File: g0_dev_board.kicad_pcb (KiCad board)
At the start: 4 copper layers, 80 x 114 mm, 198 parts, among them J201 USB_B_Mini, J202 F103_SWD, J301 USB_B_Mini, J401 RJ45_Hanrun_HR911105A_Horizon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, J501 DM3AT-SF-PEJM5, J801 Uno_IOH, J802 Uno_IOL, J803 Uno_POWER, J804 Uno_ANALOG, J805 J_LA_L, J806 J_LA_R, Q201 MMBT3904, SW701 RESET, SW702 USER, U101 STM32G0B1CCT6, U201 USBLC6-2SC6, U202 AP7361C-33E, U203 STM32F103CBTx, U301 USBLC6-2SC6, U302 FT232RL, U401 W5500, U501 W25Q32JVSSIQ, U601 TMP100, U602 TMP100, Y101 32.768kHz CL7pF, Y201 8MHz, Y401 25MHz

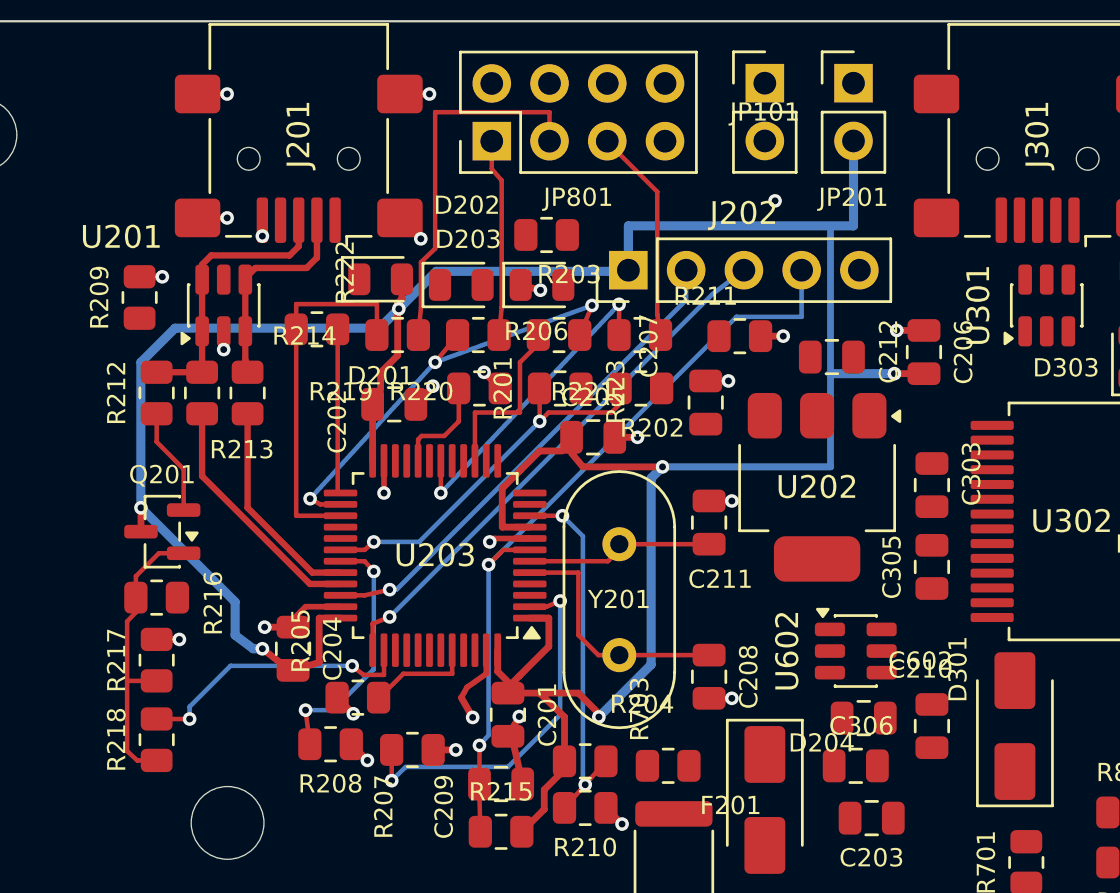
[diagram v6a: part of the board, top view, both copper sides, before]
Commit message: refactor(pcb): turn In2 into power plane with +3V3_STL island
По решению пользователя In2 стал слоем питания: +3.3V на всю плату и остров
+3V3_STL под ST-Link с выступом до JP201. In1 остаётся сплошной GND (опора
для F.Cu, дифпары не затронуты). Удалены 20 сегментов магистрали +3V3_STL на
B.Cu, которые замыкали область вокруг F103; питание выводов теперь через
переходные в остров. C206 возвращён к выводу 48. DRC: 0 нарушений.
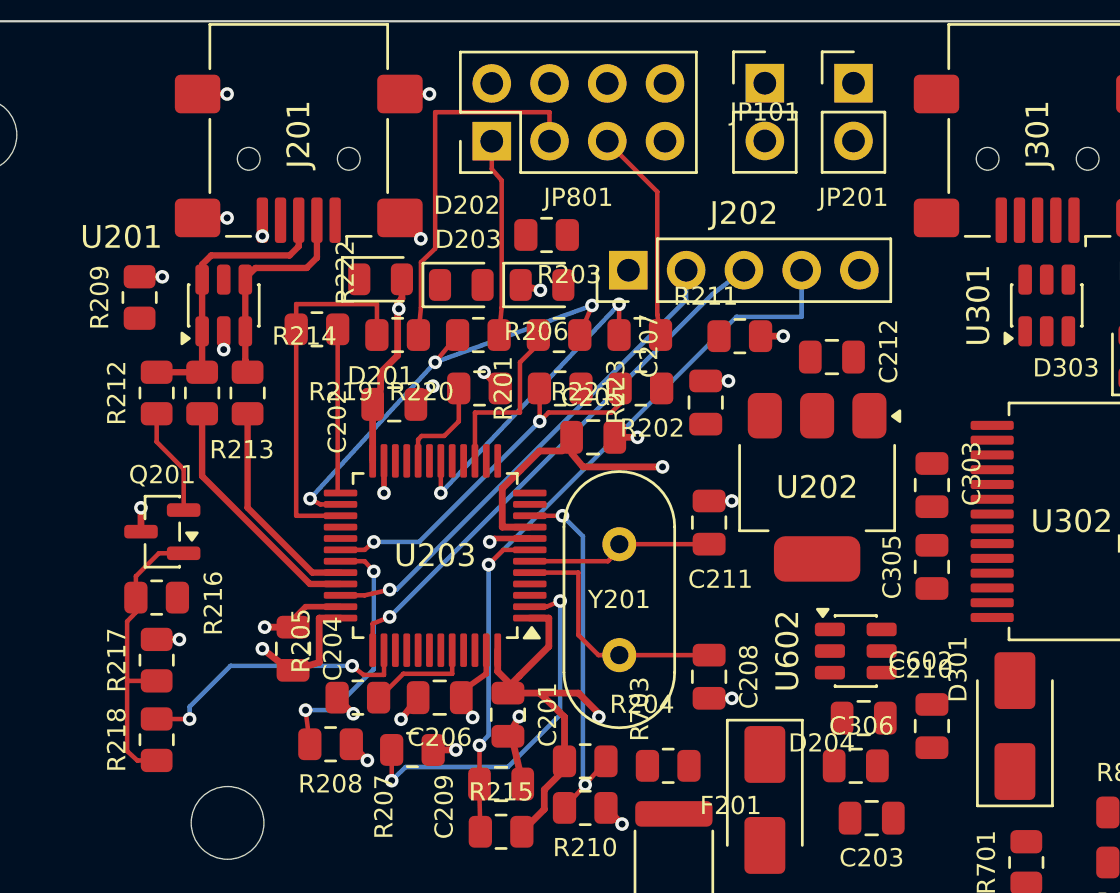
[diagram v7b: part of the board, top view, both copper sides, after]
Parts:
- moved C206 26.2 mm to (125.2, 65.8), turned to 0 degrees
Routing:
- net +3V3_STL: track 129.1 -> 42.2 mm
- net GND: track 35.6 -> 34.4 mm, vias 27 -> 25
- added copper zone on In2.Cu, net +3.3V
- added copper zone on In2.Cu, net +3V3_STL
- removed copper zone on In2.Cu, net GND
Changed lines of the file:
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@@
 	(footprint "Capacitor_SMD:C_0805_2012Metric"
 		(layer "F.Cu")
-		(at 146.5 50.55 90)
+		(at 125.2 65.75)
 		(descr "Capacitor SMD 0805 (2012 Metric), square (rectangular) end terminal, IPC-7351 nominal, (Body size source: IPC-SM-782 page 76, https://www.pcb-3d.com/wordpress/wp-content/uploads/ipc-sm-782a_amendment_1_and_2.pdf, https://docs.google.com/spreadsheets/d/1BsfQQcO9C6DZCsRaXUlFlo91Tg2WpOkGARC1WS5S8t0/edit?usp=sharing)")
 		(tags "capacitor")
 		(property "Reference" "C206"
-			(at 0 1.75 270)
+			(at 0 1.75 180)
 			(layer "F.SilkS")
 			(effects
@@
 		)
 		(property "Value" "4.7u"
-			(at 0 1.68 90)
+			(at 0 1.68 0)
 			(layer "F.Fab")
 			(effects
@@
 		)
 		(property "Datasheet" ""
-			(at 0 0 90)
+			(at 0 0 0)
 			(layer "F.Fab")
 			(hide yes)
@@
 		)
 		(property "Description" "Unpolarized capacitor"
-			(at 0 0 90)
+			(at 0 0 0)
 			(layer "F.Fab")
 			(hide yes)
@@
 		)
 		(property "KiLib_Generator" "SMD_2terminal_chip_molded"
-			(at 0 0 90)
+			(at 0 0 0)
 			(layer "F.SilkS")
 			(hide yes)
@@
 		)
 		(property "LCSC" "C1779"
-			(at 0 0 90)
+			(at 0 0 0)
 			(layer "F.SilkS")
 			(hide yes)
@@
 		)
 		(fp_text user "${REFERENCE}"
-			(at 0 0 90)
+			(at 0 0 0)
 			(layer "F.Fab")
 			(effects
@@
 		)
 		(pad "1" smd roundrect
-			(at -0.95 0 90)
+			(at -0.95 0)
 			(size 1 1.45)
 			(layers "F.Cu" "F.Mask" "F.Paste")
@@
 		)
 		(pad "2" smd roundrect
-			(at 0.95 0 90)
+			(at 0.95 0)
 			(size 1 1.45)
 			(layers "F.Cu" "F.Mask" "F.Paste")
@@
 	)
 	(segment
+		(start 124.25 65.75)
+		(end 123.5 66.7)
+		(width 0.3)
+		(layer "F.Cu")
+		(net "+3V3_STL")
+	)
+	(segment
 		(start 119.9 62.25)
 		(end 119.9 64.2)
@@
 	)
 	(segment
-		(start 146.5 51.5)
-		(end 145.2 51.5)
-		(width 0.3)
-		(layer "F.Cu")
-		(net "+3V3_STL")
-	)
-	(segment
 		(start 123.54 48.2)
 		(end 123.35 48.4)
@@
 	)
 	(via
-		(at 145.2 51.5)
-		(size 0.6)
-		(drill 0.3)
-		(layers "F.Cu" "B.Cu")
-		(net "+3V3_STL")
-	)
-	(via
 		(at 135 55.6)
 		(size 0.6)
@@
 		(net "+3V3_STL")
 	)
-	(segment
-		(start 145.2 51.5)
-		(end 142.39 51.5)
-		(width 0.4)
-		(layer "B.Cu")
-		(net "+3V3_STL")
-	)
-	(segment
-		(start 132.199999 66.599999)
-		(end 134.5 64.3)
-		(width 0.4)
-		(layer "B.Cu")
-		(net "+3V3_STL")
-	)
-	(segment
-		(start 112.06 51)
-		(end 113.56 49.5)
-		(width 0.4)
-		(layer "B.Cu")
-		(net "+3V3_STL")
-	)
-	(segment
-		(start 125.05 47)
-		(end 132.65 47)
-		(width 0.4)
-		(layer "B.Cu")
-		(net "+3V3_STL")
-	)
-	(segment
-		(start 116.2 63)
-		(end 117 63.6)
-		(width 0.4)
-		(layer "B.Cu")
-		(net "+3V3_STL")
-	)
-	(segment
-		(start 133.5 46.95)
-		(end 133.5 45)
-		(width 0.4)
-		(layer "B.Cu")
-		(net "+3V3_STL")
-	)
-	(segment
-		(start 142.39 55.6)
-		(end 142.39 45)
-		(width 0.3)
-		(layer "B.Cu")
-		(net "+3V3_STL")
-	)
-	(segment
-		(start 143.4 45)
-		(end 143.4 41.265)
-		(width 0.4)
-		(layer "B.Cu")
-		(net "+3V3_STL")
-	)
-	(segment
-		(start 117 63.6)
-		(end 117.4 63.6)
-		(width 0.4)
-		(layer "B.Cu")
-		(net "+3V3_STL")
-	)
-	(segment
-		(start 112.06 57.4)
-		(end 112.06 51)
-		(width 0.4)
-		(layer "B.Cu")
-		(net "+3V3_STL")
-	)
-	(segment
-		(start 133.5 45)
-		(end 143.4 45)
-		(width 0.4)
-		(layer "B.Cu")
-		(net "+3V3_STL")
-	)
-	(segment
-		(start 134.5 56.1)
-		(end 135 55.6)
-		(width 0.4)
-		(layer "B.Cu")
-		(net "+3V3_STL")
-	)
-	(segment
-		(start 113.56 49.5)
-		(end 122.55 49.5)
-		(width 0.4)
-		(layer "B.Cu")
-		(net "+3V3_STL")
-	)
-	(segment
-		(start 116.2 61.54)
-		(end 116.2 63)
-		(width 0.4)
-		(layer "B.Cu")
-		(net "+3V3_STL")
-	)
-	(segment
-		(start 123.4 48.65)
-		(end 125.05 47)
-		(width 0.4)
-		(layer "B.Cu")
-		(net "+3V3_STL")
-	)
-	(segment
-		(start 135 55.6)
-		(end 142.39 55.6)
-		(width 0.3)
-		(layer "B.Cu")
-		(net "+3V3_STL")
-	)
-	(segment
-		(start 112.06 57.4)
-		(end 116.2 61.54)
-		(width 0.4)
-		(layer "B.Cu")
-		(net "+3V3_STL")
-	)
-	(segment
-		(start 134.5 64.3)
-		(end 134.5 56.1)
-		(width 0.4)
-		(layer "B.Cu")
-		(net "+3V3_STL")
-	)
-	(segment
-		(start 132.65 47)
-		(end 133.5 46.95)
-		(width 0.4)
-		(layer "B.Cu")
-		(net "+3V3_STL")
-	)
-	(segment
-		(start 122.55 49.5)
-		(end 123.4 48.65)
-		(width 0.4)
-		(layer "B.Cu")
+	(via
+		(at 123.5 66.7)
+		(size 0.6)
+		(drill 0.3)
+		(layers "F.Cu" "B.Cu")
 		(net "+3V3_STL")
 	)
@@
 	)
 	(segment
-		(start 146.5 49.6)
-		(end 145.3 49.6)
-		(width 0.3)
-		(layer "F.Cu")
-		(net "GND")
-	)
-	(segment
 		(start 115.7 49.638)
 		(end 115.7 50.44)
@@
 	)
 	(via
-		(at 139.95 43.9)
-		(size 0.6)
-		(drill 0.3)
-		(layers "F.Cu" "B.Cu")
-		(net "GND")
-	)
-	(via
 		(at 138.05 57.1)
 		(size 0.6)
@@
 	)
 	(via
-		(at 145.3 49.6)
-		(size 0.6)
-		(drill 0.3)
-		(layers "F.Cu" "B.Cu")
-		(net "GND")
-	)
-	(via
 		(at 138.05 65.78)
 		(size 0.6)
@@
 	)
 	(zone
-		(net "GND")
+		(net "+3.3V")
 		(layer "In2.Cu")
 		(hatch edge 0.5)
@@
 		(polygon
 			(pts
-				(xy 100.3 36.3) (xy 179.7 36.3) (xy 179.7 149.7) (xy 100.3 149.7)
+				(xy 100.3 36.3) (xy 110 36.3) (xy 110 73.1) (xy 137 73.1) (xy 137 46.2) (xy 145.2 46.2) (xy 145.2 39.3)
+				(xy 141.4 39.3) (xy 141.4 42.4) (xy 137 42.4) (xy 137 36.3) (xy 179.7 36.3) (xy 179.7 149.7) (xy 100.3 149.7)
+			)
+		)
+	)
+	(zone
+		(net "+3V3_STL")
+		(layer "In2.Cu")
+		(hatch edge 0.5)
+		(connect_pads
+			(clearance 0.25)
+		)
+		(min_thickness 0.2)
+		(fill
+			(thermal_gap 0.5)
+			(thermal_bridge_width 0.5)
+			(island_removal_mode 0)
+		)
+		(polygon
+			(pts
+				(xy 110.6 36.3) (xy 136.4 36.3) (xy 136.4 43) (xy 142 43) (xy 142 39.9) (xy 144.6 39.9) (xy 144.6 45.6)
+				(xy 136.4 45.6) (xy 136.4 72.5) (xy 110.6 72.5)
 			)
 		)

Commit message: feat(pcb): rework ST-Link LED cluster and JP801 SWD lines
R201/R202/R211 перенесены к светодиодам у верхнего края (R201/R202
вертикально), D201/D202 сдвинуты; D203/R203 (индикатор основной +3.3V)
перенесены к LDO, так как зона под ST-Link теперь остров +3V3_STL.
/STL_SWDIO и /STL_SWCLK к JP801 переведены на B.Cu, связка SWCLK
R220<->R223 сделана по F.Cu (R220 повёрнут). LED_STLINK идёт на B.Cu
через зазор между выводами J202. DRC: 0 ошибок, 2 предупреждения о
переходных посреди цепочек на B.Cu (уберу при чистке).
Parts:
- moved D203 18.2 mm to (147.2, 52.7), turned to 90 degrees
- moved R203 16.9 mm to (146.2, 49.9)
- moved R211 15.7 mm to (122.9, 47.4), turned to 180 degrees
- moved R202 10.6 mm to (126.3, 44.8), turned to -90 degrees
- moved R201 7.34 mm to (129.8, 44.8), turned to -90 degrees
- moved D201 7.25 mm to (129.8, 47.6)
- moved D202 0.20 mm to (126.3, 47.6)
- turned R220 to 180 degrees
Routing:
- net /st_link/LED_STLINK: track 17.1 -> 31.3 mm, vias 2 -> 3
- net GND: track 34.4 -> 39.3 mm, vias 25 -> 24
- net Net-(D202-A): track 0.00 -> 2.18 mm
- net Net-(D201-K): track 0.00 -> 2.16 mm
- net Net-(D203-A): track 0.00 -> 1.91 mm
- net Net-(D202-K): track 0.00 -> 1.62 mm
- net /st_link/STL_SWCLK: track 19.8 -> 18.5 mm
- net +3V3_STL: track 42.2 -> 43.5 mm, vias 6 -> 7
- net +3.3V: track 0.00 -> 0.89 mm, vias 0 -> 1
- net /STL_SWDIO: track 16.4 -> 16.8 mm, vias 0 -> 1
- net /STL_SWCLK: track 8.69 -> 9.09 mm, vias 0 -> 1
